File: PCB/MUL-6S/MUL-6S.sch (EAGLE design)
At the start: 22 parts

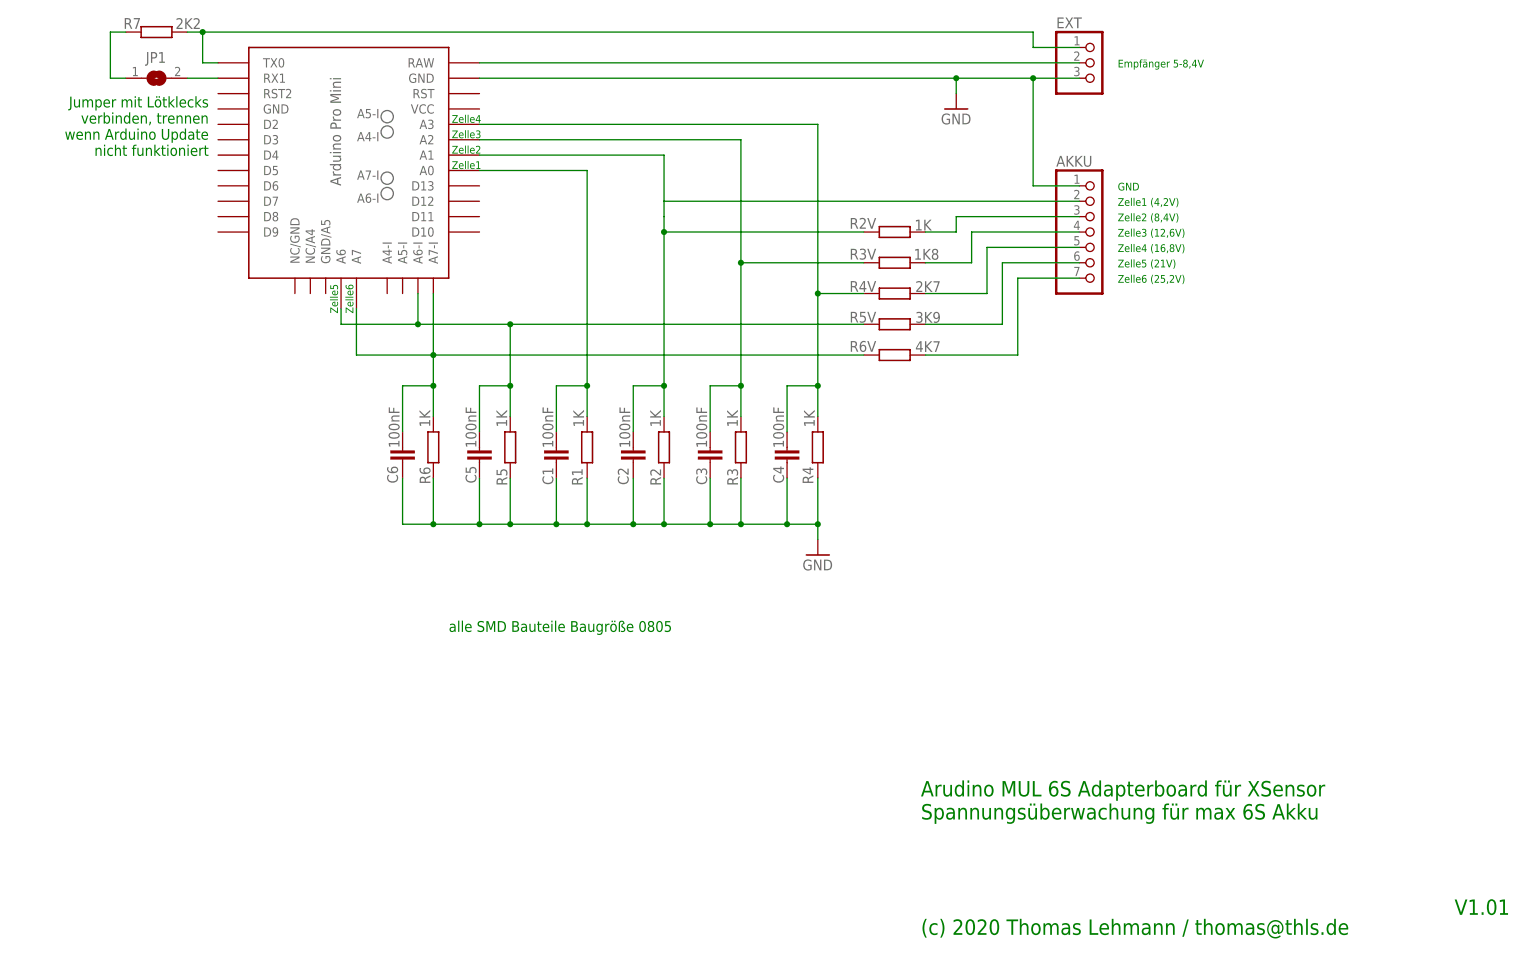
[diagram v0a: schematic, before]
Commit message: Zelle 1 war falsch angeschlossen
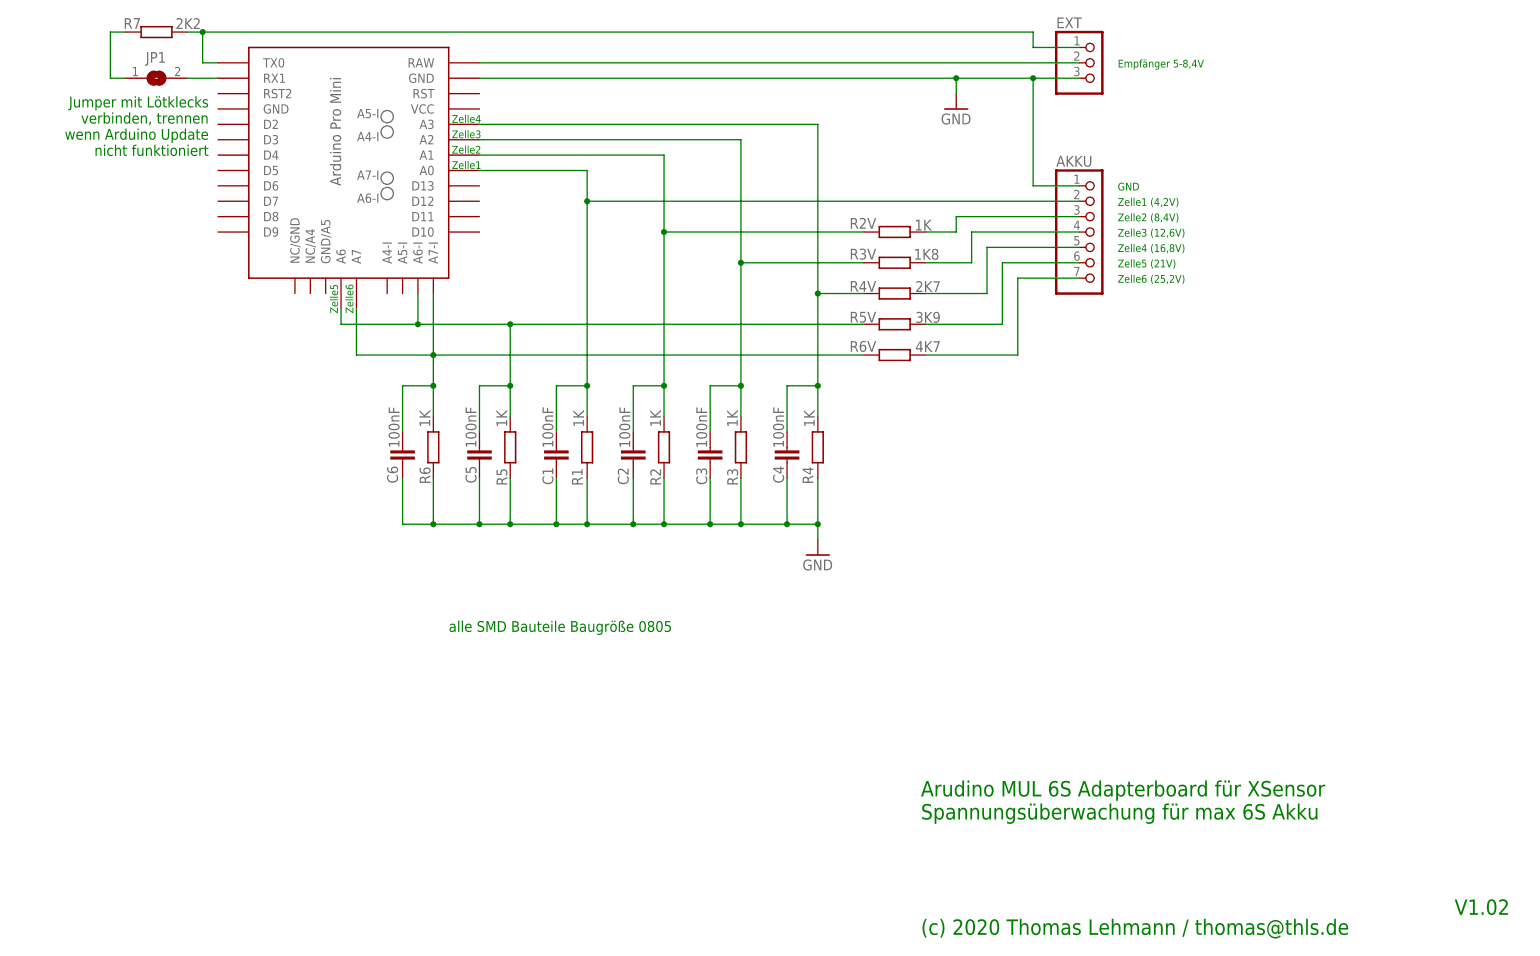
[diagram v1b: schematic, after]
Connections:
- net N$10: now also AKKU.2
- net N$19: no longer AKKU.2
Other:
- note added: "V1.02"
- note removed: "V1.01"
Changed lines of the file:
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@@
 <text x="164.338" y="3.302" size="2.54" layer="91">(c) 2020 Thomas Lehmann / thomas@thls.de
 </text>
-<text x="252.476" y="6.604" size="2.54" layer="91">V1.01</text>
+<text x="252.476" y="6.604" size="2.54" layer="91">V1.02</text>
 <text x="46.736" y="141.732" size="1.778" layer="91" rot="R180">Jumper mit Lötklecks
 verbinden, trennen
@@
 <wire x1="109.22" y1="129.54" x2="91.44" y2="129.54" width="0.1524" layer="91"/>
 <pinref part="R1" gate="G$1" pin="1"/>
-<wire x1="109.22" y1="129.54" x2="109.22" y2="93.98" width="0.1524" layer="91"/>
+<wire x1="109.22" y1="129.54" x2="109.22" y2="124.46" width="0.1524" layer="91"/>
+<wire x1="109.22" y1="124.46" x2="109.22" y2="93.98" width="0.1524" layer="91"/>
 <wire x1="109.22" y1="88.9" x2="109.22" y2="93.98" width="0.1524" layer="91"/>
 <pinref part="C1" gate="G$1" pin="1"/>
@@
 <wire x1="104.14" y1="93.98" x2="109.22" y2="93.98" width="0.1524" layer="91"/>
 <junction x="109.22" y="93.98"/>
+<pinref part="AKKU" gate="A" pin="2"/>
+<wire x1="190.5" y1="124.46" x2="109.22" y2="124.46" width="0.1524" layer="91"/>
+<junction x="109.22" y="124.46"/>
 </segment>
 </net>
@@
 <pinref part="C2" gate="G$1" pin="1"/>
 <wire x1="121.92" y1="93.98" x2="121.92" y2="119.38" width="0.1524" layer="91"/>
-<wire x1="121.92" y1="119.38" x2="121.92" y2="121.92" width="0.1524" layer="91"/>
-<wire x1="121.92" y1="124.46" x2="121.92" y2="132.08" width="0.1524" layer="91"/>
+<wire x1="121.92" y1="119.38" x2="121.92" y2="132.08" width="0.1524" layer="91"/>
 <wire x1="116.84" y1="86.36" x2="116.84" y2="93.98" width="0.1524" layer="91"/>
 <wire x1="116.84" y1="93.98" x2="121.92" y2="93.98" width="0.1524" layer="91"/>
@@
 <wire x1="154.94" y1="119.38" x2="121.92" y2="119.38" width="0.1524" layer="91"/>
 <junction x="121.92" y="119.38"/>
-<pinref part="AKKU" gate="A" pin="2"/>
-<wire x1="190.5" y1="124.46" x2="121.92" y2="124.46" width="0.1524" layer="91"/>
-<wire x1="121.92" y1="124.46" x2="121.92" y2="121.92" width="0.1524" layer="91"/>
 </segment>
 </net>
